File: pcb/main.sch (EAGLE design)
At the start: 222 parts

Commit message: updated schematic for main board
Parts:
- removed C13, C14, C15, C16, C17, C18, C19, C20, C21, C22, C23, C24, C25, C26, C27, C28, C29, C30, C31, C32, C33, C34, C35, C36, C37, C38, C39, C40, C41, C42, C43, C44, C45, C46, C47, C48, C49, C50, C51, C52, C53, C54, C55, C56, C57, C58, C59, C60, C61, C62, C63, C64, C65, C66, C67, C68: (no value), rcl:C-EUC1206
- removed C69, C71, C72: (no value), rcl:CPOL-EU153CLV-0605
- removed LED1, LED10, LED100, LED101, LED102, LED103, LED104, LED105, LED106, LED107, LED108, LED109, LED11, LED110, LED111, LED112, LED113, LED114, LED115, LED116, LED117, LED118, LED119, LED12, LED120, LED121, LED122, LED123, LED124, LED125, LED126, LED127, LED128, LED129, LED13, LED14, LED15, LED16, LED17, LED18, LED19, LED2, LED20, LED21, LED22, LED23, LED24, LED25, LED26, LED27, LED28, LED29, LED3, LED30, LED31, LED32, LED33, LED34, LED35, LED36, LED37, LED38, LED39, LED4, LED40, LED41, LED42, LED43, LED44, LED45, LED46, LED47, LED48, LED49, LED5, LED50, LED51, LED52, LED53, LED54, LED55, LED56, LED57, LED58, LED59, LED6, LED60, LED61, LED62, LED63, LED64, LED65, LED66, LED67, LED68, LED69, LED7, LED70, LED71, LED72, LED73, LED74, LED75, LED76, LED77, LED78, LED79, LED8, LED80, LED81, LED82, LED83, LED84, LED85, LED86, LED87, LED88, LED89, LED9, LED90, LED91, LED92, LED93, LED94, LED95, LED96, LED97, LED98, LED99: APA102, adafruit:APA102
- removed R49, R50, R51, R52: 10k, rcl:R-EU_M1206
- removed R53, R56: 120R, rcl:R-EU_M1206
- removed R55: 390R, rcl:R-EU_M1206
- removed SL1: (no value), con-amp-quick:M06
- removed SL2: (no value), con-amp-quick:M02
- removed U$12, U$13, U$14, U$15, U$16: 74HCT125D, SparkFun-DigitalIC:74HCT125D
- added C4: (no value), rcl:CPOL-EUE3.5-8
- added D1: 1N5400, diode:1N5400
- added IC2, IC3, IC4: 74HCT04N, 74xx-eu:74HCT04N
- added U$5: DCDC, main:DCDC
- added U$6: ESP32DEVKITV1, ESP32-DEVKITV1:ESP32DEVKITV1
- added U$7, U$8: LEDCON, main:LEDCON
- C1, C6, C7: device rcl:CPOL-EU153CLV-0605 -> rcl:CPOL-EUE3.5-8
- C10, C11, C3, C9: device rcl:C-EUC1206 -> rcl:CPOL-EUE3.5-8
- C12, C2, C5: device rcl:C-EUC1206 -> rcl:C-EU025_050-025X075
- C8: device rcl:CPOL-EU153CLV-0405 -> rcl:C-EU025_050-025X075
- IC1: value (none) -> 74HCT04N; device v-reg:LM317TS -> 74xx-eu:74HCT04N
- U$1: value ESP07-16PIN -> DCDC; device esp8266modules:ESP07-16PIN -> main:DCDC
- U$10, U$9: value 74HCT125D -> LEDCON; device SparkFun-DigitalIC:74HCT125D -> main:LEDCON
- U$11: value 74HCT125D -> TX30; device SparkFun-DigitalIC:74HCT125D -> main:TX30
- U$2: value CMODS6 -> CMODS6TH; device main:CMODS6 -> main:CMODS6TH
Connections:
- removed net +3V3: C3.1, C5.1, C8.+, IC1.OUT, R49.2, R51.2, R52.2, R53.2, U$1.VCC
- removed net GA1: U$2.8, U$9.1A
- removed net GA2: U$2.9, U$9.2A
- removed net GA3: U$2.10, U$9.3A
- removed net GA4: U$2.11, U$9.4A
- removed net GA5: U$10.1A, U$2.12
- removed net GA6: U$10.2A, U$2.13
- removed net GA7: U$10.3A, U$2.14
- removed net GA8: U$10.4A, U$2.15
- removed net GB1: U$11.1A, U$2.33
- removed net GB2: U$11.2A, U$2.32
- removed net GB3: U$11.3A, U$2.31
- removed net GB4: U$11.4A, U$2.30
- removed net GB5: U$12.1A, U$2.16
- removed net GB6: U$12.2A, U$2.17
- removed net GB7: U$12.3A, U$2.18
- removed net GB8: U$12.4A, U$2.19
- removed net GC1: U$13.1A, U$2.29
- removed net GC2: U$13.2A, U$2.28
- removed net GC3: U$13.3A, U$2.27
- removed net GC4: U$13.4A, U$2.26
- removed net GC5: U$14.1A, U$2.20
- removed net GC6: U$14.2A, U$2.21
- removed net GC7: U$14.3A, U$2.22
- removed net GC8: U$14.4A, U$2.23
- removed net GD1: U$15.1A, U$2.41
- removed net GD2: U$15.2A, U$2.40
- removed net GD3: U$15.3A, U$2.39
- removed net GD4: U$15.4A, U$2.38
- removed net GD5: U$16.1A, U$2.37
- removed net GD6: U$16.2A, U$2.36
- removed net GD7: U$16.3A, U$2.35
- removed net GD8: U$16.4A, U$2.34
- removed net GPIO0: R51.1, SL1.1, U$1.GPIO0, U$2.5
- removed net GPIO12: U$1.GPIO12, U$2.46
- removed net GPIO13: U$1.GPIO13, U$2.45
- removed net GPIO14: U$1.GPIO14, U$2.47
- removed net GPIO15: R50.2, U$1.GPIO15, U$2.7
- removed net GPIO16: U$1.GPIO16, U$2.48
- removed net GPIO2: U$1.GPIO2, U$2.6
- removed net GPIO4: U$1.GPIO4, U$2.3
- removed net GPIO5: U$1.GPIO5, U$2.4
- removed net N$100: LED23.DO, LED24.DI
- removed net N$101: LED23.CO, LED24.CI
- removed net N$102: LED20.DO, LED21.DI
- removed net N$103: LED20.CO, LED21.CI
- removed net N$104: LED35.DO, LED36.DI
- removed net N$105: LED24.DO, LED25.DI
- removed net N$106: LED24.CO, LED25.CI
- removed net N$107: LED25.DO, LED26.DI
- removed net N$108: LED25.CO, LED26.CI
- removed net N$109: LED26.DO, LED27.DI
- removed net N$112: LED26.CO, LED27.CI
- removed net N$113: LED27.DO, LED28.DI
- removed net N$114: LED27.CO, LED28.CI
- removed net N$115: LED28.DO, LED29.DI
- removed net N$116: IC1.ADJ, R55.2, R56.1
- removed net N$117: LED28.CO, LED29.CI
- removed net N$118: R53.1, R56.2
- removed net N$119: LED29.DO, LED30.DI
- removed net N$120: LED29.CO, LED30.CI
- removed net N$123: LED1.DI, U$9.1Y
- removed net N$162: LED30.DO, LED31.DI
- removed net N$163: LED30.CO, LED31.CI
- removed net N$164: LED31.DO, LED32.DI
- removed net N$165: LED31.CO, LED32.CI
- removed net N$166: LED32.DO, LED33.DI
- removed net N$167: LED32.CO, LED33.CI
- removed net N$168: LED1.CI, U$9.2Y
- removed net N$169: LED6.DI, U$9.3Y
- removed net N$170: LED6.CI, U$9.4Y
- removed net N$171: LED12.DI, U$10.1Y
- removed net N$172: LED12.CI, U$10.2Y
- removed net N$173: LED20.DI, U$10.3Y
- removed net N$174: LED20.CI, U$10.4Y
- removed net N$180: LED35.CO, LED36.CI
- removed net N$181: LED36.DO, LED37.DI
- removed net N$183: LED36.CO, LED37.CI
- removed net N$184: LED37.DO, LED38.DI
- removed net N$185: LED37.CO, LED38.CI
- removed net N$186: LED34.DO, LED35.DI
- removed net N$187: LED34.CO, LED35.CI
- removed net N$188: LED40.DO, LED41.DI
- removed net N$189: LED40.CO, LED41.CI
- removed net N$190: LED41.DO, LED42.DI
- removed net N$191: LED41.CO, LED42.CI
- removed net N$192: LED42.DO, LED43.DI
- removed net N$193: LED42.CO, LED43.CI
- removed net N$194: LED39.DO, LED40.DI
- removed net N$195: LED39.CO, LED40.CI
- removed net N$196: LED43.DO, LED44.DI
- removed net N$197: LED43.CO, LED44.CI
- removed net N$198: LED46.DO, LED47.DI
- removed net N$199: LED46.CO, LED47.CI
- removed net N$200: LED47.DO, LED48.DI
- removed net N$201: LED47.CO, LED48.CI
- removed net N$202: LED48.DO, LED49.DI
- removed net N$203: LED48.CO, LED49.CI
- removed net N$204: LED45.DO, LED46.DI
- removed net N$205: LED45.CO, LED46.CI
- removed net N$206: LED49.DO, LED50.DI
- removed net N$207: LED49.CO, LED50.CI
- removed net N$208: LED50.DO, LED51.DI
- removed net N$209: LED50.CO, LED51.CI
- removed net N$210: LED51.DO, LED52.DI
- removed net N$211: LED51.CO, LED52.CI
- removed net N$212: LED54.DO, LED55.DI
- removed net N$213: LED54.CO, LED55.CI
- removed net N$214: LED55.DO, LED56.DI
- removed net N$215: LED55.CO, LED56.CI
- removed net N$216: LED56.DO, LED57.DI
- removed net N$217: LED56.CO, LED57.CI
- removed net N$218: LED53.DO, LED54.DI
- removed net N$219: LED53.CO, LED54.CI
- removed net N$220: LED57.DO, LED58.DI
- removed net N$221: LED57.CO, LED58.CI
- removed net N$222: LED58.DO, LED59.DI
- removed net N$223: LED58.CO, LED59.CI
- removed net N$224: LED59.DO, LED60.DI
- removed net N$225: LED59.CO, LED60.CI
- removed net N$226: LED60.DO, LED61.DI
- removed net N$227: LED60.CO, LED61.CI
- removed net N$228: LED61.DO, LED62.DI
- removed net N$229: LED61.CO, LED62.CI
- removed net N$230: LED62.DO, LED63.DI
- removed net N$231: LED62.CO, LED63.CI
- removed net N$232: LED63.DO, LED64.DI
- removed net N$233: LED63.CO, LED64.CI
- removed net N$234: LED64.DO, LED65.DI
- removed net N$235: LED64.CO, LED65.CI
- removed net N$236: LED67.DO, LED68.DI
- removed net N$237: LED67.CO, LED68.CI
- removed net N$238: LED34.DI, U$11.1Y
- removed net N$239: LED34.CI, U$11.2Y
- removed net N$240: LED39.DI, U$11.3Y
- removed net N$241: LED39.CI, U$11.4Y
- removed net N$242: LED45.DI, U$12.1Y
- removed net N$243: LED45.CI, U$12.2Y
- removed net N$244: LED53.DI, U$12.3Y
- removed net N$245: LED53.CI, U$12.4Y
- removed net N$255: LED68.DO, LED69.DI
- removed net N$256: LED68.CO, LED69.CI
- removed net N$257: LED69.DO, LED70.DI
- removed net N$258: LED69.CO, LED70.CI
- removed net N$259: LED66.DO, LED67.DI
- removed net N$260: LED66.CO, LED67.CI
- removed net N$261: LED72.DO, LED73.DI
- removed net N$262: LED72.CO, LED73.CI
- removed net N$263: LED73.DO, LED74.DI
- removed net N$264: LED73.CO, LED74.CI
- removed net N$265: LED74.DO, LED75.DI
- removed net N$266: LED74.CO, LED75.CI
- removed net N$267: LED71.DO, LED72.DI
- removed net N$268: LED71.CO, LED72.CI
- removed net N$269: LED75.DO, LED76.DI
- removed net N$270: LED75.CO, LED76.CI
- removed net N$271: LED78.DO, LED79.DI
- removed net N$272: LED78.CO, LED79.CI
- removed net N$273: LED79.DO, LED80.DI
- removed net N$274: LED79.CO, LED80.CI
- removed net N$275: LED80.DO, LED81.DI
- removed net N$276: LED80.CO, LED81.CI
- removed net N$277: LED77.DO, LED78.DI
- removed net N$278: LED77.CO, LED78.CI
- removed net N$279: LED81.DO, LED82.DI
- removed net N$280: LED81.CO, LED82.CI
- removed net N$281: LED82.DO, LED83.DI
- removed net N$282: LED82.CO, LED83.CI
- removed net N$283: LED83.DO, LED84.DI
- removed net N$284: LED83.CO, LED84.CI
- removed net N$285: LED86.DO, LED87.DI
- removed net N$286: LED86.CO, LED87.CI
- removed net N$287: LED87.DO, LED88.DI
- removed net N$288: LED87.CO, LED88.CI
- removed net N$289: LED88.DO, LED89.DI
- removed net N$290: LED88.CO, LED89.CI
- removed net N$291: LED85.DO, LED86.DI
- removed net N$292: LED85.CO, LED86.CI
- removed net N$293: LED89.DO, LED90.DI
- removed net N$294: LED89.CO, LED90.CI
- removed net N$295: LED90.DO, LED91.DI
- removed net N$296: LED90.CO, LED91.CI
- removed net N$297: LED91.DO, LED92.DI
- removed net N$298: LED91.CO, LED92.CI
- removed net N$299: LED92.DO, LED93.DI
- removed net N$300: LED92.CO, LED93.CI
- removed net N$301: LED93.DO, LED94.DI
- removed net N$302: LED93.CO, LED94.CI
- removed net N$303: LED94.DO, LED95.DI
- removed net N$304: LED94.CO, LED95.CI
- removed net N$305: LED95.DO, LED96.DI
- removed net N$306: LED95.CO, LED96.CI
- removed net N$307: LED96.DO, LED97.DI
- removed net N$308: LED96.CO, LED97.CI
- removed net N$309: LED66.DI, U$13.1Y
- removed net N$310: LED66.CI, U$13.2Y
- removed net N$311: LED71.DI, U$13.3Y
- removed net N$312: LED71.CI, U$13.4Y
- removed net N$313: LED77.DI, U$14.1Y
- removed net N$314: LED77.CI, U$14.2Y
- removed net N$315: LED85.DI, U$14.3Y
- removed net N$316: LED85.CI, U$14.4Y
- removed net N$326: LED100.DI, LED99.DO
- removed net N$327: LED100.CI, LED99.CO
- removed net N$328: LED100.DO, LED101.DI
- removed net N$329: LED100.CO, LED101.CI
- removed net N$330: LED101.DO, LED102.DI
- removed net N$331: LED101.CO, LED102.CI
- removed net N$332: LED98.DO, LED99.DI
- removed net N$333: LED98.CO, LED99.CI
- removed net N$334: LED104.DO, LED105.DI
- removed net N$335: LED104.CO, LED105.CI
- removed net N$336: LED105.DO, LED106.DI
- removed net N$337: LED105.CO, LED106.CI
- removed net N$338: LED106.DO, LED107.DI
- removed net N$339: LED106.CO, LED107.CI
- removed net N$340: LED103.DO, LED104.DI
- removed net N$341: LED103.CO, LED104.CI
- removed net N$342: LED107.DO, LED108.DI
- removed net N$343: LED107.CO, LED108.CI
- removed net N$344: LED110.DO, LED111.DI
- removed net N$345: LED110.CO, LED111.CI
- removed net N$346: LED111.DO, LED112.DI
- removed net N$347: LED111.CO, LED112.CI
- removed net N$348: LED112.DO, LED113.DI
- removed net N$349: LED112.CO, LED113.CI
- removed net N$350: LED109.DO, LED110.DI
- removed net N$351: LED109.CO, LED110.CI
- removed net N$352: LED113.DO, LED114.DI
- removed net N$353: LED113.CO, LED114.CI
- removed net N$354: LED114.DO, LED115.DI
- removed net N$355: LED114.CO, LED115.CI
- removed net N$356: LED115.DO, LED116.DI
- removed net N$357: LED115.CO, LED116.CI
- removed net N$358: LED118.DO, LED119.DI
- removed net N$359: LED118.CO, LED119.CI
- removed net N$360: LED119.DO, LED120.DI
- removed net N$361: LED119.CO, LED120.CI
- removed net N$362: LED120.DO, LED121.DI
- removed net N$363: LED120.CO, LED121.CI
- removed net N$364: LED117.DO, LED118.DI
- removed net N$365: LED117.CO, LED118.CI
- removed net N$366: LED121.DO, LED122.DI
- removed net N$367: LED121.CO, LED122.CI
- removed net N$368: LED122.DO, LED123.DI
- removed net N$369: LED122.CO, LED123.CI
- removed net N$370: LED123.DO, LED124.DI
- removed net N$371: LED123.CO, LED124.CI
- removed net N$372: LED124.DO, LED125.DI
- removed net N$373: LED124.CO, LED125.CI
- removed net N$374: LED125.DO, LED126.DI
- removed net N$375: LED125.CO, LED126.CI
- removed net N$376: LED126.DO, LED127.DI
- removed net N$377: LED126.CO, LED127.CI
- removed net N$378: LED127.DO, LED128.DI
- removed net N$379: LED127.CO, LED128.CI
- removed net N$380: LED128.DO, LED129.DI
- removed net N$381: LED128.CO, LED129.CI
- removed net N$382: LED98.DI, U$15.1Y
- removed net N$383: LED98.CI, U$15.2Y
- removed net N$384: LED103.DI, U$15.3Y
- removed net N$385: LED103.CI, U$15.4Y
- removed net N$386: LED109.DI, U$16.1Y
- removed net N$387: LED109.CI, U$16.2Y
- removed net N$388: LED117.DI, U$16.3Y
- removed net N$389: LED117.CI, U$16.4Y
- removed net N$46: LED2.DO, LED3.DI
- removed net N$51: LED2.CO, LED3.CI
- removed net N$56: LED3.DO, LED4.DI
- removed net N$57: LED3.CO, LED4.CI
- removed net N$58: LED4.DO, LED5.DI
- removed net N$59: LED4.CO, LED5.CI
- removed net N$60: LED1.DO, LED2.DI
- removed net N$61: LED1.CO, LED2.CI
- removed net N$66: LED7.DO, LED8.DI
- removed net N$67: LED7.CO, LED8.CI
- removed net N$68: LED8.DO, LED9.DI
- removed net N$69: LED8.CO, LED9.CI
- removed net N$70: LED10.DI, LED9.DO
- removed net N$71: LED10.CI, LED9.CO
- removed net N$72: LED6.DO, LED7.DI
- removed net N$73: LED6.CO, LED7.CI
- removed net N$75: LED10.DO, LED11.DI
- removed net N$76: LED10.CO, LED11.CI
- removed net N$77: LED21.DO, LED22.DI
- removed net N$78: LED13.DO, LED14.DI
- removed net N$80: LED13.CO, LED14.CI
- removed net N$82: LED14.DO, LED15.DI
- removed net N$83: R52.1, SL1.5, U$1.RESET
- removed net N$84: R49.1, U$1.CH_PD
- removed net N$85: LED14.CO, LED15.CI
- removed net N$86: LED15.DO, LED16.DI
- removed net N$87: LED15.CO, LED16.CI
- removed net N$88: LED12.DO, LED13.DI
- removed net N$89: LED12.CO, LED13.CI
- removed net N$91: LED16.DO, LED17.DI
- removed net N$92: LED16.CO, LED17.CI
- removed net N$93: LED21.CO, LED22.CI
- removed net N$94: LED17.DO, LED18.DI
- removed net N$95: LED17.CO, LED18.CI
- removed net N$96: LED22.DO, LED23.DI
- removed net N$97: LED18.DO, LED19.DI
- removed net N$98: LED18.CO, LED19.CI
- removed net N$99: LED22.CO, LED23.CI
- removed net RX: SL1.3, U$1.RX, U$2.2
- removed net TX: SL1.2, U$1.TX, U$2.1
- new net +5V/3: C10.+, C8.1, IC3P.VCC, U$4.VOUT
- new net +5V/4: C11.+, C12.1, IC4P.VCC, U$5.VOUT
- new net C1: IC1E.I, IC1F.I, U$2.14
- new net C2: IC2E.I, IC2F.I, U$2.19
- new net C3: IC3E.I, IC3F.I, U$2.35
- new net C4: IC4E.I, IC4F.I, U$2.30
- new net D11: IC1A.I, U$2.15
- new net D12: IC1B.I, U$2.16
- new net D13: IC1C.I, U$2.17
- new net D14: IC1D.I, U$2.18
- new net D21: IC2A.I, U$2.20
- new net D22: IC2B.I, U$2.21
- new net D23: IC2C.I, U$2.22
- new net D24: IC2D.I, U$2.23
- new net D31: IC3A.I, U$2.34
- new net D32: IC3B.I, U$2.33
- new net D33: IC3C.I, U$2.32
- new net D34: IC3D.I, U$2.31
- new net D41: IC4A.I, U$2.29
- new net D42: IC4B.I, U$2.28
- new net D43: IC4C.I, U$2.27
- new net D44: IC4D.I, U$2.26
- new net IO13: U$2.48, U$6.IO13
- new net IO14: U$2.47, U$6.IO14
- new net IO15: U$2.1, U$6.IO15
- new net IO16: U$2.3, U$6.IO16
- new net IO17: U$2.4, U$6.IO17
- new net IO18: U$2.6, U$6.IO18
- new net IO19: U$2.7, U$6.IO19
- new net IO21: U$2.8, U$6.IO21
- new net IO22: U$2.9, U$6.IO22
- new net IO23: U$2.10, U$6.IO23
- new net IO25: U$2.44, U$6.IO25
- new net IO26: U$2.45, U$6.IO26
- new net IO27: U$2.46, U$6.IO27
- new net IO32: U$2.42, U$6.IO32
- new net IO33: U$2.43, U$6.IO33
- new net IO4: U$2.2, U$6.IO4
- new net IO5: U$2.5, U$6.IO5
- new net N$10: IC2B.O, U$8.D2
- new net N$11: IC2A.O, U$8.D1
- new net N$12: IC2E.O, U$8.C3, U$8.C4
- new net N$13: IC2F.O, U$8.C1, U$8.C2
- new net N$14: IC3D.O, U$9.D4
- new net N$15: IC3C.O, U$9.D3
- new net N$16: IC3B.O, U$9.D2
- new net N$17: IC3A.O, U$9.D1
- new net N$18: IC3E.O, U$9.C3, U$9.C4
- new net N$19: IC3F.O, U$9.C1, U$9.C2
- new net N$2: IC1D.O, U$7.D4
- new net N$20: IC4D.O, U$10.D4
- new net N$21: IC4C.O, U$10.D3
- new net N$22: IC4B.O, U$10.D2
- new net N$23: IC4A.O, U$10.D1
- new net N$24: IC4E.O, U$10.C3, U$10.C4
- new net N$25: IC4F.O, U$10.C1, U$10.C2
- new net N$26: D1.A, U$11.P
- new net N$3: IC1C.O, U$7.D3
- new net N$4: IC1B.O, U$7.D2
- new net N$5: IC1A.O, U$7.D1
- new net N$6: IC1E.O, U$7.C3, U$7.C4
- new net N$7: IC1F.O, U$7.C1, U$7.C2
- new net N$8: IC2D.O, U$8.D4
- new net N$9: IC2C.O, U$8.D3
- net +12V: now also C3.+, D1.C, SL3.1, U$1.VIN, U$3.VIN, U$4.VIN, U$5.VIN, U$6.VIN; no longer C2.1, C69.+, C71.+, C72.+, IC1.IN, SL2.2, U$3.VIN1, U$3.VIN2, U$4.VIN1, U$4.VIN2
- net +5V/1: now also C2.1, C4.+, IC1P.VCC, U$1.VOUT; no longer C10.1, C11.1, C12.1, C13.1, C14.1, C15.1, C16.1, C17.1, C18.1, C19.1, C20.1, C21.1, C22.1, C23.1, C24.1, C25.1, C26.1, C27.1, C28.1, C29.1, C30.1, C31.1, C32.1, C33.1, C34.1, C35.1, C36.1, C37.1, C38.1, C9.1, LED1.VCC, LED10.VCC, LED11.VCC, LED12.VCC, LED13.VCC, LED14.VCC, LED15.VCC, LED16.VCC, LED17.VCC, LED18.VCC, LED19.VCC, LED2.VCC, LED20.VCC, LED21.VCC, LED22.VCC, LED23.VCC, LED24.VCC, LED25.VCC, LED26.VCC, LED27.VCC, LED28.VCC, LED29.VCC, LED3.VCC, LED30.VCC, LED31.VCC, LED32.VCC, LED33.VCC, LED34.VCC, LED35.VCC, LED36.VCC, LED37.VCC, LED38.VCC, LED39.VCC, LED4.VCC, LED40.VCC, LED41.VCC, LED42.VCC, LED43.VCC, LED44.VCC, LED45.VCC, LED46.VCC, LED47.VCC, LED48.VCC, LED49.VCC, LED5.VCC, LED50.VCC, LED51.VCC, LED52.VCC, LED53.VCC, LED54.VCC, LED55.VCC, LED56.VCC, LED57.VCC, LED58.VCC, LED59.VCC, LED6.VCC, LED60.VCC, LED61.VCC, LED62.VCC, LED63.VCC, LED64.VCC, LED65.VCC, LED7.VCC, LED8.VCC, LED9.VCC, SL3.1, U$10.VCC, U$11.VCC, U$12.VCC, U$3.VOUT1, U$3.VOUT2, U$9.VCC
- net +5V/2: now also C5.1, C9.+, IC2P.VCC, U$3.VOUT; no longer C39.1, C40.1, C41.1, C42.1, C43.1, C44.1, C45.1, C46.1, C47.1, C48.1, C49.1, C50.1, C51.1, C52.1, C53.1, C54.1, C55.1, C56.1, C57.1, C58.1, C59.1, C60.1, C61.1, C62.1, C63.1, C64.1, C65.1, C66.1, C67.1, C68.1, LED100.VCC, LED101.VCC, LED102.VCC, LED103.VCC, LED104.VCC, LED105.VCC, LED106.VCC, LED107.VCC, LED108.VCC, LED109.VCC, LED110.VCC, LED111.VCC, LED112.VCC, LED113.VCC, LED114.VCC, LED115.VCC, LED116.VCC, LED117.VCC, LED118.VCC, LED119.VCC, LED120.VCC, LED121.VCC, LED122.VCC, LED123.VCC, LED124.VCC, LED125.VCC, LED126.VCC, LED127.VCC, LED128.VCC, LED129.VCC, LED66.VCC, LED67.VCC, LED68.VCC, LED69.VCC, LED70.VCC, LED71.VCC, LED72.VCC, LED73.VCC, LED74.VCC, LED75.VCC, LED76.VCC, LED77.VCC, LED78.VCC, LED79.VCC, LED80.VCC, LED81.VCC, LED82.VCC, LED83.VCC, LED84.VCC, LED85.VCC, LED86.VCC, LED87.VCC, LED88.VCC, LED89.VCC, LED90.VCC, LED91.VCC, LED92.VCC, LED93.VCC, LED94.VCC, LED95.VCC, LED96.VCC, LED97.VCC, LED98.VCC, LED99.VCC, U$13.VCC, U$14.VCC, U$15.VCC, U$16.VCC, U$4.VOUT1, U$4.VOUT2
- net GND: now also C10.-, C11.-, C3.-, C4.-, C8.2, C9.-, IC1P.GND, IC2P.GND, IC3P.GND, IC4P.GND, SL3.2, U$11.N, U$3.GND, U$4.GND, U$5.GND, U$6.GND, U$6.GND1; no longer C10.2, C11.2, C13.2, C14.2, C15.2, C16.2, C17.2, C18.2, C19.2, C20.2, C21.2, C22.2, C23.2, C24.2, C25.2, C26.2, C27.2, C28.2, C29.2, C3.2, C30.2, C31.2, C32.2, C33.2, C34.2, C35.2, C36.2, C37.2, C38.2, C39.2, C40.2, C41.2, C42.2, C43.2, C44.2, C45.2, C46.2, C47.2, C48.2, C49.2, C50.2, C51.2, C52.2, C53.2, C54.2, C55.2, C56.2, C57.2, C58.2, C59.2, C60.2, C61.2, C62.2, C63.2, C64.2, C65.2, C66.2, C67.2, C68.2, C69.-, C71.-, C72.-, C8.-, C9.2, LED1.GND, LED10.GND, LED100.GND, LED101.GND, LED102.GND, LED103.GND, LED104.GND, LED105.GND, LED106.GND, LED107.GND, LED108.GND, LED109.GND, LED11.GND, LED110.GND, LED111.GND, LED112.GND, LED113.GND, LED114.GND, LED115.GND, LED116.GND, LED117.GND, LED118.GND, LED119.GND, LED12.GND, LED120.GND, LED121.GND, LED122.GND, LED123.GND, LED124.GND, LED125.GND, LED126.GND, LED127.GND, LED128.GND, LED129.GND, LED13.GND, LED14.GND, LED15.GND, LED16.GND, LED17.GND, LED18.GND, LED19.GND, LED2.GND, LED20.GND, LED21.GND, LED22.GND, LED23.GND, LED24.GND, LED25.GND, LED26.GND, LED27.GND, LED28.GND, LED29.GND, LED3.GND, LED30.GND, LED31.GND, LED32.GND, LED33.GND, LED34.GND, LED35.GND, LED36.GND, LED37.GND, LED38.GND, LED39.GND, LED4.GND, LED40.GND, LED41.GND, LED42.GND, LED43.GND, LED44.GND, LED45.GND, LED46.GND, LED47.GND, LED48.GND, LED49.GND, LED5.GND, LED50.GND, LED51.GND, LED52.GND, LED53.GND, LED54.GND, LED55.GND, LED56.GND, LED57.GND, LED58.GND, LED59.GND, LED6.GND, LED60.GND, LED61.GND, LED62.GND, LED63.GND, LED64.GND, LED65.GND, LED66.GND, LED67.GND, LED68.GND, LED69.GND, LED7.GND, LED70.GND, LED71.GND, LED72.GND, LED73.GND, LED74.GND, LED75.GND, LED76.GND, LED77.GND, LED78.GND, LED79.GND, LED8.GND, LED80.GND, LED81.GND, LED82.GND, LED83.GND, LED84.GND, LED85.GND, LED86.GND, LED87.GND, LED88.GND, LED89.GND, LED9.GND, LED90.GND, LED91.GND, LED92.GND, LED93.GND, LED94.GND, LED95.GND, LED96.GND, LED97.GND, LED98.GND, LED99.GND, R50.1, R55.1, SL1.6, SL2.1, SL3.3, U$10.1OE, U$10.2OE, U$10.3OE, U$10.4OE, U$10.GND, U$11.1OE, U$11.2OE, U$11.3OE, U$11.4OE, U$11.GND, U$12.1OE, U$12.2OE, U$12.3OE, U$12.4OE, U$12.GND, U$13.1OE, U$13.2OE, U$13.3OE, U$13.4OE, U$13.GND, U$14.1OE, U$14.2OE, U$14.3OE, U$14.4OE, U$14.GND, U$15.1OE, U$15.2OE, U$15.3OE, U$15.4OE, U$15.GND, U$16.1OE, U$16.2OE, U$16.3OE, U$16.4OE, U$16.GND, U$3.GND1, U$3.GND2, U$3.GND3, U$3.GND4, U$4.GND1, U$4.GND2, U$4.GND3, U$4.GND4, U$9.1OE, U$9.2OE, U$9.3OE, U$9.4OE, U$9.GND
- net N$1: now also SL3.3, U$2.36; no longer SL3.2, U$2.44

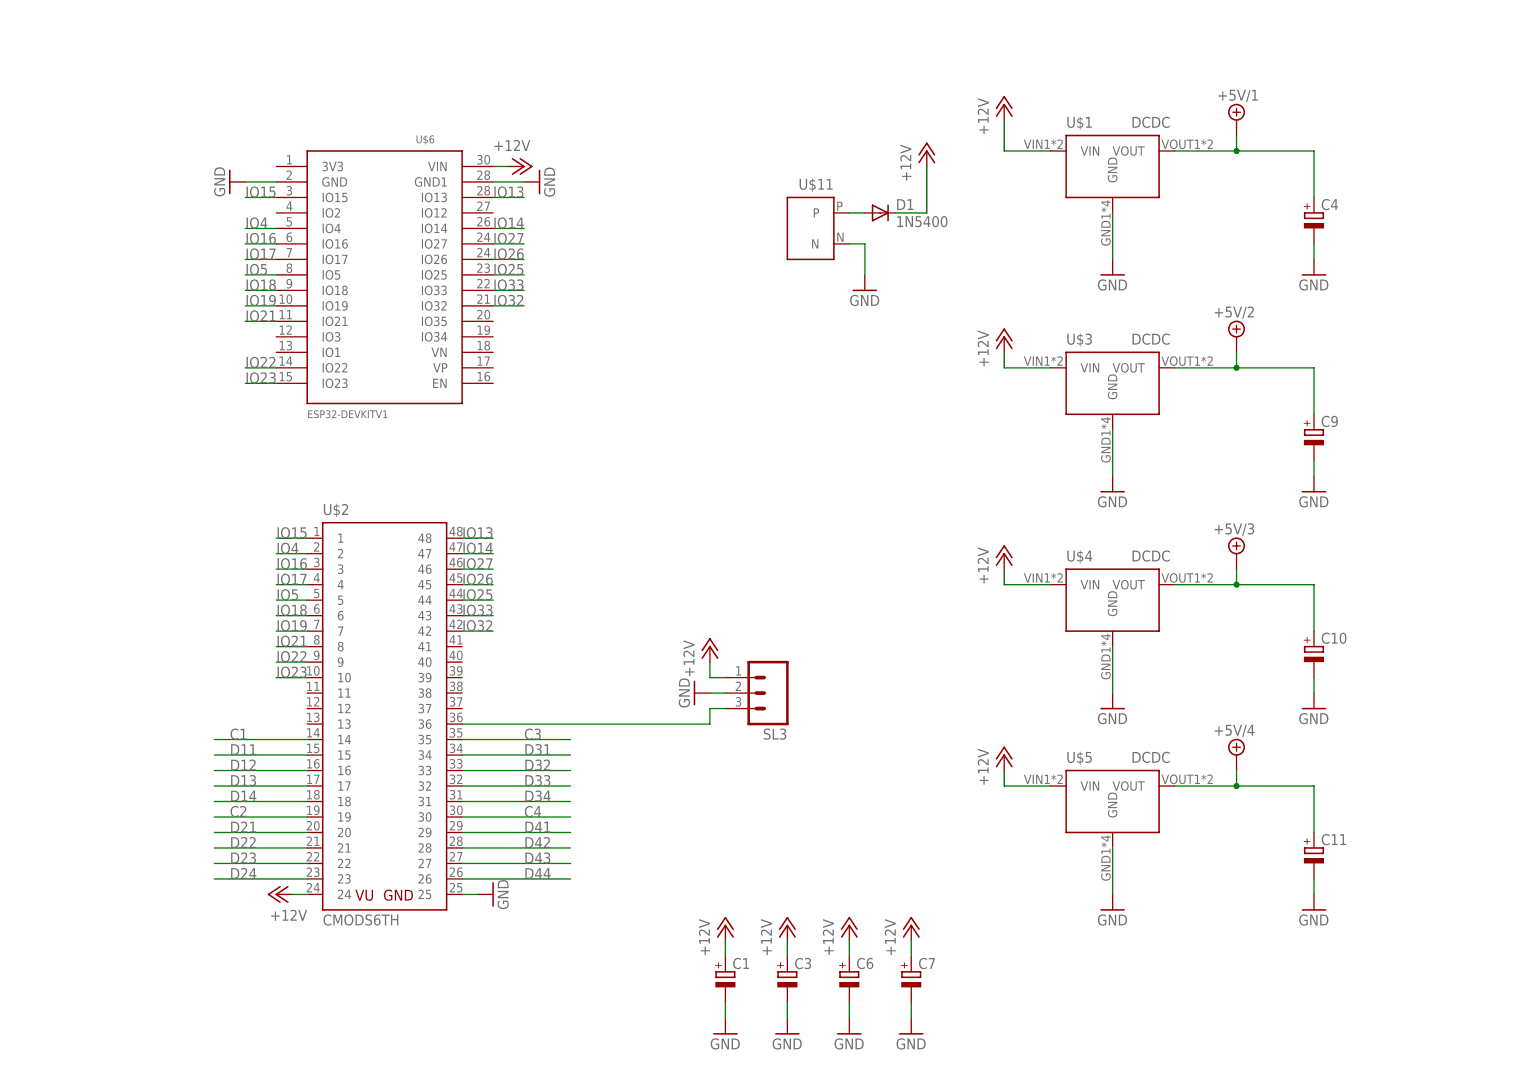
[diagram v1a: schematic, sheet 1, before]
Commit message: updated schematic for motor driver
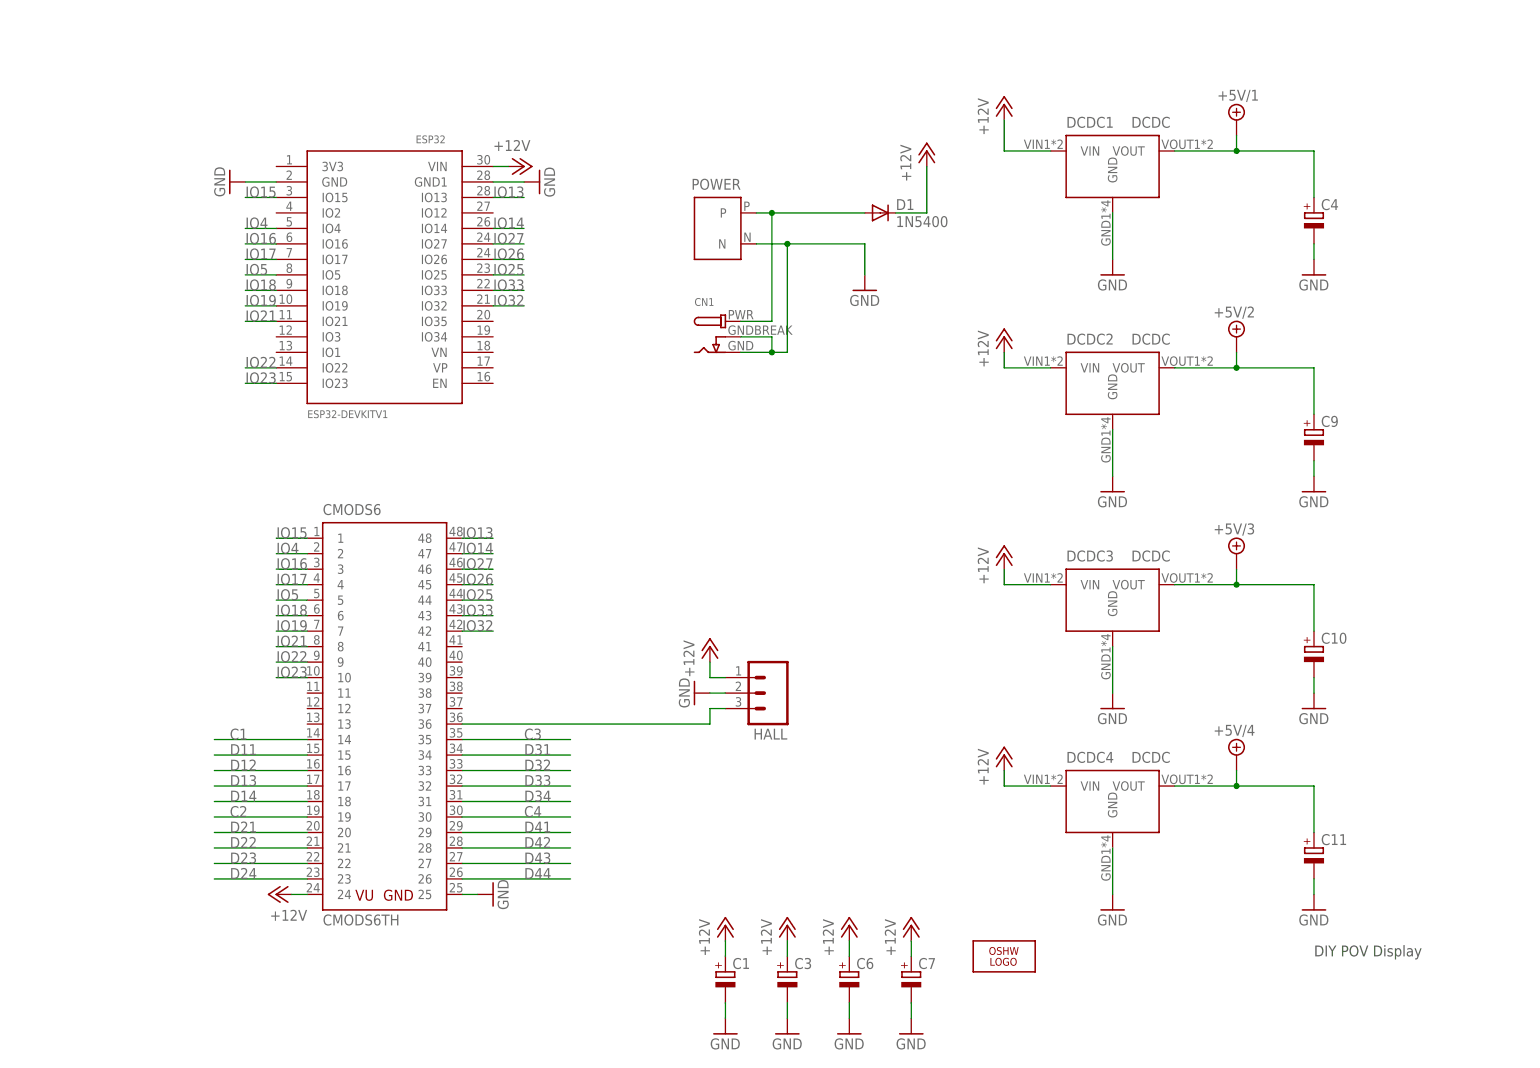
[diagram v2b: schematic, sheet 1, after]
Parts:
- removed U$11: TX30, main:TX30
- added CN1: (no value), microbuilder:DCBARRELPTH
- added LOGO1: OSHW_LOGO_FILLX0350-NT, ohw-logo:OSHW_LOGO_FILLX0350-NT
- added POWER: TX30, main:TX30
- renumbered SL3 to HALL, U$1 to DCDC1, U$10 to LEDS4, U$2 to CMODS6, U$3 to DCDC2, U$4 to DCDC3, U$5 to DCDC4, U$6 to ESP32, U$7 to LEDS1, U$8 to LEDS2, U$9 to LEDS3
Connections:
- net GND: now also CN1.GND, CN1.GNDBREAK, POWER.N; no longer U$11.N
- net N$26: now also CN1.PWR, POWER.P; no longer U$11.P
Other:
- note added: "DIY POV Display"

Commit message: first version of motor driver pcb layout
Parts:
- added U$1: LOGO50MM, im-pro-logo:LOGO50MM
- CMODS6: device main:CMODS6TH -> diypov:CMODS6TH
- DCDC1, DCDC2, DCDC3, DCDC4: value DCDC -> DCDC_5V; device main:DCDC -> diypov:DCDC_5V
- HALL: value (none) -> HALL; device con-amp-quick:M03 -> diypov:HALL
- LEDS1, LEDS2, LEDS3, LEDS4: device main:LEDCON -> diypov:LEDCON
- POWER: device main:TX30 -> diypov:TX30
- renumbered CN1 to POWER_TEST
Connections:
- new net IO1: CMODS6.11, ESP32.IO1
- new net IO12: CMODS6.47, ESP32.IO12
- new net IO2: CMODS6.2, ESP32.IO2
- new net IO3: CMODS6.10, ESP32.IO3
- new net IO34: CMODS6.39, ESP32.IO34
- new net IO35: CMODS6.40, ESP32.IO35
- new net IO36: CMODS6.37, ESP32.VP
- new net IO39: CMODS6.38, ESP32.VN
- net +12V: now also HALL.VCC; no longer HALL.1
- net GND: now also HALL.GND; no longer HALL.2
- net IO14: now also CMODS6.46; no longer CMODS6.47
- net IO16: now also CMODS6.4; no longer CMODS6.3
- net IO17: now also CMODS6.5; no longer CMODS6.4
- net IO18: now also CMODS6.7; no longer CMODS6.6
- net IO19: now also CMODS6.8; no longer CMODS6.7
- net IO21: now also CMODS6.9; no longer CMODS6.8
- net IO22: now also CMODS6.12; no longer CMODS6.9
- net IO23: now also CMODS6.13; no longer CMODS6.10
- net IO25: now also CMODS6.43; no longer CMODS6.44
- net IO26: now also CMODS6.44; no longer CMODS6.45
- net IO27: now also CMODS6.45; no longer CMODS6.46
- net IO32: now also CMODS6.41; no longer CMODS6.42
- net IO33: now also CMODS6.42; no longer CMODS6.43
- net IO4: now also CMODS6.3; no longer CMODS6.2
- net IO5: now also CMODS6.6; no longer CMODS6.5
- net N$1: now also HALL.OUT; no longer HALL.3

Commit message: started layout of main pcb
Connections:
- net +5V/1: now also LEDS1.VCC
- net +5V/2: now also LEDS2.VCC
- net +5V/3: now also LEDS3.VCC
- net +5V/4: now also LEDS4.VCC
- net GND: now also LEDS1.GND, LEDS2.GND, LEDS3.GND, LEDS4.GND

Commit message: first version layout main pcb
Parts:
- removed ESP32: ESP32DEVKITV1, ESP32-DEVKITV1:ESP32DEVKITV1
- added U$2: ESP32DEVKITV1, ESP32-DEVKITV1:ESP32DEVKITV1
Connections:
- removed net IO13: CMODS6.48, ESP32.IO13
- net +12V: now also U$2.VIN; no longer ESP32.VIN
- net C1: now also CMODS6.35; no longer CMODS6.14
- net C2: now also CMODS6.5, IC2A.I, IC2B.I; no longer CMODS6.19, IC2E.I, IC2F.I
- net C3: now also CMODS6.48, IC3A.I; no longer CMODS6.35, IC3E.I
- net C4: now also CMODS6.29; no longer CMODS6.30
- net D11: now also CMODS6.39, IC1C.I; no longer CMODS6.15, IC1A.I
- net D12: now also CMODS6.37; no longer CMODS6.16
- net D13: now also CMODS6.34, IC1A.I; no longer CMODS6.17, IC1C.I
- net D14: now also CMODS6.38; no longer CMODS6.18
- net D21: now also CMODS6.4, IC2C.I; no longer CMODS6.20, IC2A.I
- net D22: now also CMODS6.3, IC2F.I; no longer CMODS6.21, IC2B.I
- net D23: now also CMODS6.2, IC2E.I; no longer CMODS6.22, IC2C.I
- net D24: now also CMODS6.1; no longer CMODS6.23
- net D31: now also CMODS6.47, IC3B.I; no longer CMODS6.34, IC3A.I
- net D32: now also CMODS6.45, IC3C.I; no longer CMODS6.33, IC3B.I
- net D33: now also CMODS6.46, IC3E.I; no longer CMODS6.32, IC3C.I
- net D34: now also CMODS6.44; no longer CMODS6.31
- net D41: now also CMODS6.28; no longer CMODS6.29
- net D42: now also CMODS6.27; no longer CMODS6.28
- net D43: now also CMODS6.26; no longer CMODS6.27
- net D44: now also CMODS6.30; no longer CMODS6.26
- net GND: now also U$2.GND, U$2.GND1; no longer ESP32.GND, ESP32.GND1
- net IO1: now also CMODS6.20, U$2.IO1; no longer CMODS6.11, ESP32.IO1
- net IO12: now also CMODS6.7, U$2.IO12; no longer CMODS6.47, ESP32.IO12
- net IO14: now also CMODS6.8, U$2.IO14; no longer CMODS6.46, ESP32.IO14
- net IO15: now also CMODS6.6, U$2.IO15; no longer CMODS6.1, ESP32.IO15
- net IO16: now also CMODS6.41, U$2.IO16; no longer CMODS6.4, ESP32.IO16
- net IO17: now also CMODS6.40, U$2.IO17; no longer CMODS6.5, ESP32.IO17
- net IO18: now also CMODS6.16, U$2.IO18; no longer CMODS6.7, ESP32.IO18
- net IO19: now also CMODS6.33, U$2.IO19; no longer CMODS6.8, ESP32.IO19
- net IO2: now also CMODS6.43, U$2.IO2; no longer CMODS6.2, ESP32.IO2
- net IO21: now also CMODS6.32, U$2.IO21; no longer CMODS6.9, ESP32.IO21
- net IO22: now also CMODS6.22, U$2.IO22; no longer CMODS6.12, ESP32.IO22
- net IO23: now also CMODS6.23, U$2.IO23; no longer CMODS6.13, ESP32.IO23
- net IO25: now also CMODS6.12, U$2.IO25; no longer CMODS6.43, ESP32.IO25
- net IO26: now also CMODS6.10, U$2.IO26; no longer CMODS6.44, ESP32.IO26
- net IO27: now also CMODS6.9, U$2.IO27; no longer CMODS6.45, ESP32.IO27
- net IO3: now also CMODS6.31, U$2.IO3; no longer CMODS6.10, ESP32.IO3
- net IO32: now also CMODS6.15, U$2.IO32; no longer CMODS6.41, ESP32.IO32
- net IO33: now also CMODS6.36, U$2.IO33; no longer CMODS6.42, ESP32.IO33
- net IO34: now also CMODS6.18, U$2.IO34; no longer CMODS6.39, ESP32.IO34
- net IO35: now also CMODS6.17, U$2.IO35; no longer CMODS6.40, ESP32.IO35
- net IO36: now also CMODS6.21, U$2.VP; no longer CMODS6.37, ESP32.VP
- net IO39: now also CMODS6.19, U$2.VN; no longer CMODS6.38, ESP32.VN
- net IO4: now also CMODS6.42, U$2.IO4; no longer CMODS6.3, ESP32.IO4
- net IO5: now also CMODS6.11, U$2.IO5; no longer CMODS6.6, ESP32.IO5
- net N$1: now also CMODS6.13; no longer CMODS6.36
- net N$10: now also IC2F.O; no longer IC2B.O
- net N$11: now also IC2C.O; no longer IC2A.O
- net N$12: now also IC2B.O; no longer IC2E.O
- net N$13: now also IC2A.O; no longer IC2F.O
- net N$15: now also IC3E.O; no longer IC3C.O
- net N$16: now also IC3C.O; no longer IC3B.O
- net N$17: now also IC3B.O; no longer IC3A.O
- net N$18: now also IC3A.O; no longer IC3E.O
- net N$24: now also IC4F.O; no longer IC4E.O
- net N$25: now also IC4E.O; no longer IC4F.O
- net N$3: now also IC1A.O; no longer IC1C.O
- net N$5: now also IC1C.O; no longer IC1A.O
- net N$6: now also IC1F.O; no longer IC1E.O
- net N$7: now also IC1E.O; no longer IC1F.O
- net N$9: now also IC2E.O; no longer IC2C.O
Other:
- moved on the sheet: IC1A, IC1C, IC1E, IC1F, IC2A, IC2B, IC2C, IC2E, IC2F, IC3A, IC3B, IC3C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
